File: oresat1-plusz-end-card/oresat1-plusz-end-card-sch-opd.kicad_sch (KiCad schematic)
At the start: 60 parts, among them Q1 DMP2240UDM-7, Q11 DMP2240UDM-7, Q2 DMN3028LQ-7, Q3 DMN3028LQ-7, Q4 DMN3028LQ-7, Q6 DMN3028LQ-7, Q9 DMP2240UDM-7, U11 MIC842LYC5, U12 MIC842LYC5, U2 MAX7310, U201 TS5A21366, U202 TS5A21366, U203 TS5A21366, U204 TS5A21366

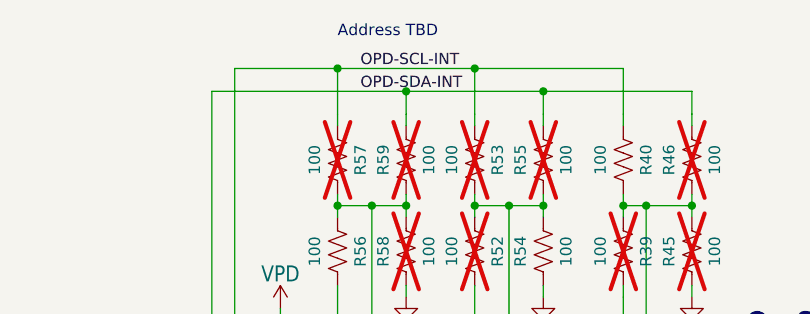
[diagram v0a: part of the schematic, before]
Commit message: Changes to minus Z
Resolved 2 git issues. Added led test light to deployer circuit to test deployment
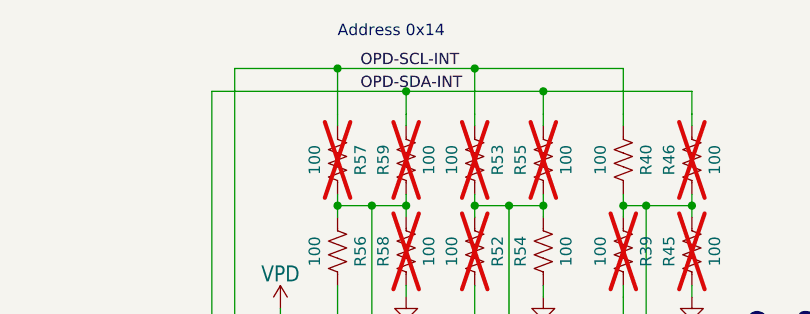
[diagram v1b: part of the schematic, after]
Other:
- note added: "Address 0x14"
- note removed: "Address TBD"

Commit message: Routine push
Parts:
- removed C202: 100n, oresat-passives:0603-C-NOSILK, symbol Device:C_Small
- removed U202, U204: TS5A21366, Package_SO:VSSOP-8_2.3x2mm_P0.5mm, symbol oresat-ics:TS5A21366
- added D1: RED, LED_SMD:LED_0603_1608Metric, symbol Device:LED_Small_Filled
- added R103, R104, R105: 10k, Resistor_SMD:R_0603_1608Metric, symbol Device:R_Small_US
- added R106: 0, oresat-passives:1206-C, symbol Device:R_Small_US
- added R107: 4.7k, oresat-passives:0603-C-NOSILK, symbol Device:R_Small_US
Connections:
- net GND: now also D1.1 (K); no longer C204.2
- net HELICAL_DEPLOY: now also R106.1, R107.1; no longer R1.2
- net VBUS: now also C204.2, R103.1
- net at Q11.1 (G), Q11.3 (G), Q9.1 (G)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: now also C204.1, R103.2, R104.1, R105.1; no longer Q2.3 (D), Q4.3 (D)
- net MY_UART_EN: no longer names the net of U2.12 (IO7)
- net MY_UART_EN: no longer C204.1
- net PY_UART_EN: no longer names the net of U2.10 (IO5)
- new net: D1.2 (A), R107.2
- new net: Q2.3 (D), Q4.3 (D), R104.2, R105.2
- new net: R1.2, R106.2
- no-connect marks 0 -> 2
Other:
- note added: "DNP for testing Install for flight"
- moved on the sheet: C203, Q11A, Q11B, Q9A, Q9B, R1, R99, U203
